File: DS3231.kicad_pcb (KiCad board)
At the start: 2 copper layers, 22.9 x 17.8 mm, 9 parts, among them IC1 DS3231, J1 Conn_01x08_Pin

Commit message: changed pin header orientation
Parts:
- J1: moved to B.Cu
- turned J1 to -90 degrees

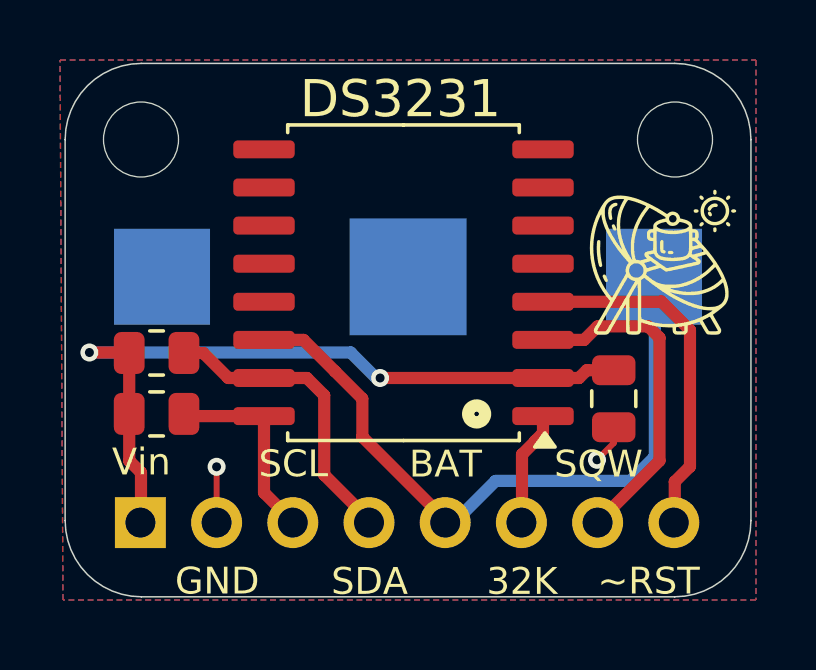
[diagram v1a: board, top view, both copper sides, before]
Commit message: CR1220 footprint update
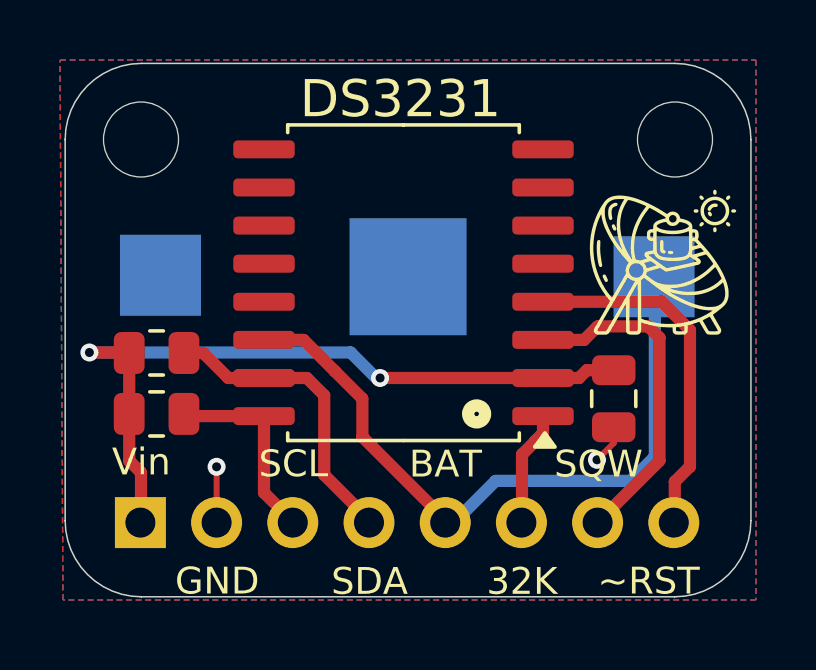
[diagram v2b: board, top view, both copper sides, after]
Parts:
- B1: footprint external_footprints:CR1220-SMD -> external_footprints:CR1220
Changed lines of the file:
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@@
 		)
 	)
-	(footprint "external_footprints:CR1220-SMD"
+	(footprint "external_footprints:CR1220"
 		(layer "B.Cu")
 		(at 148.5011 103.2256 180)
 		(property "Reference" "B1"
-			(at 0.5511 6.0256 180)
+			(at 0.635 6.4402 180)
 			(layer "B.SilkS")
 			(hide yes)
@@
 			)
 		)
-		(property "Footprint" "external_footprints:CR1220-SMD"
+		(property "Footprint" "external_footprints:CR1220"
 			(at 0 0 0)
 			(unlocked yes)
@@
 			(layer "B.SilkS")
 		)
-		(fp_circle
-			(center 8.4 0.154)
-			(end 9.3158 0.154)
-			(stroke
-				(width 0.127)
-				(type solid)
-			)
-			(fill none)
-			(layer "B.SilkS")
-		)
-		(fp_circle
-			(center -8.254 0)
-			(end -7.3382 0)
-			(stroke
-				(width 0.127)
-				(type solid)
-			)
-			(fill none)
-			(layer "B.SilkS")
-		)
 		(pad "" smd rect
-			(at 8.2 0 180)
-			(size 3.2 3.2)
+			(at 8.25 0.05 180)
+			(size 2.7 2.7)
 			(layers "B.Cu" "B.Paste" "B.Mask")
 			(solder_mask_margin 0.102)
@@
 		(pad "1" smd rect
 			(at -8.2 0 180)
-			(size 3.2 3.2)
+			(size 2.7 2.7)
 			(layers "B.Cu" "B.Paste" "B.Mask")
 			(net 5 "/VBAT")
